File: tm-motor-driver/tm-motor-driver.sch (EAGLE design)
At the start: 17 parts

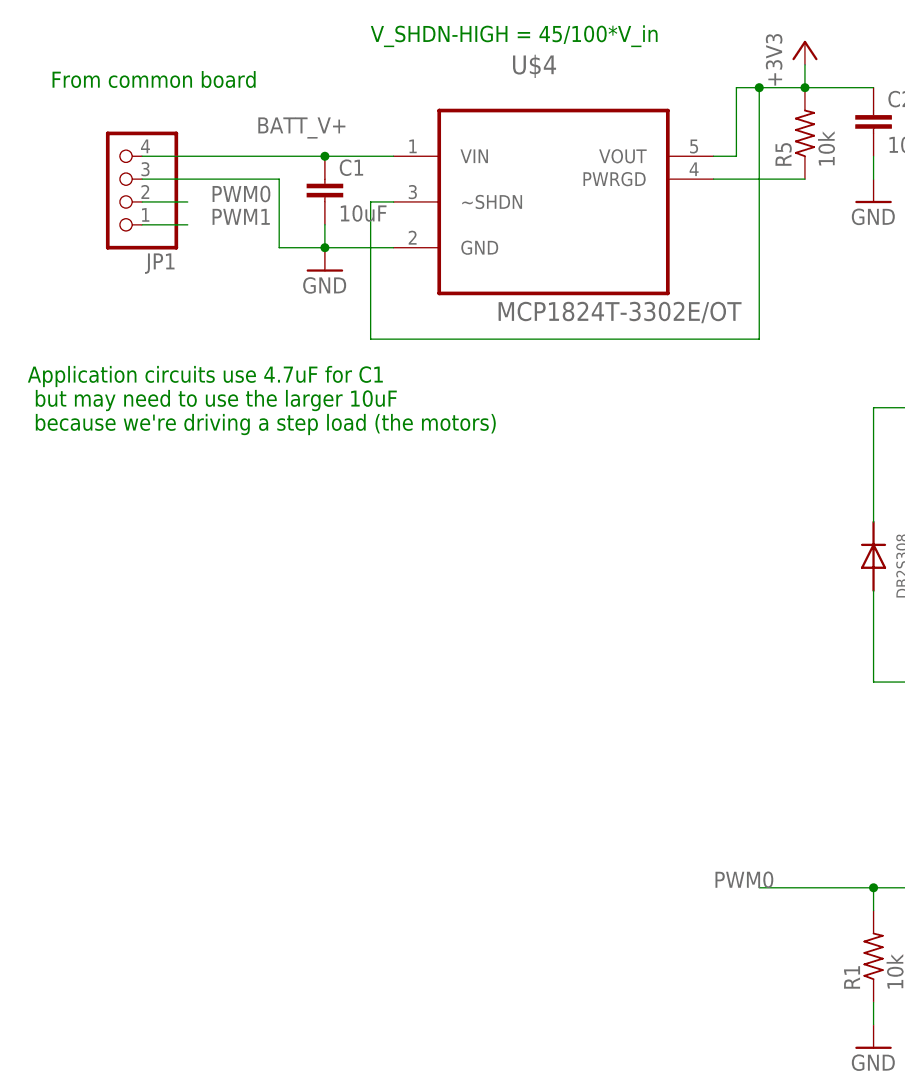
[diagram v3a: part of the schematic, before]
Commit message: Change header to JST
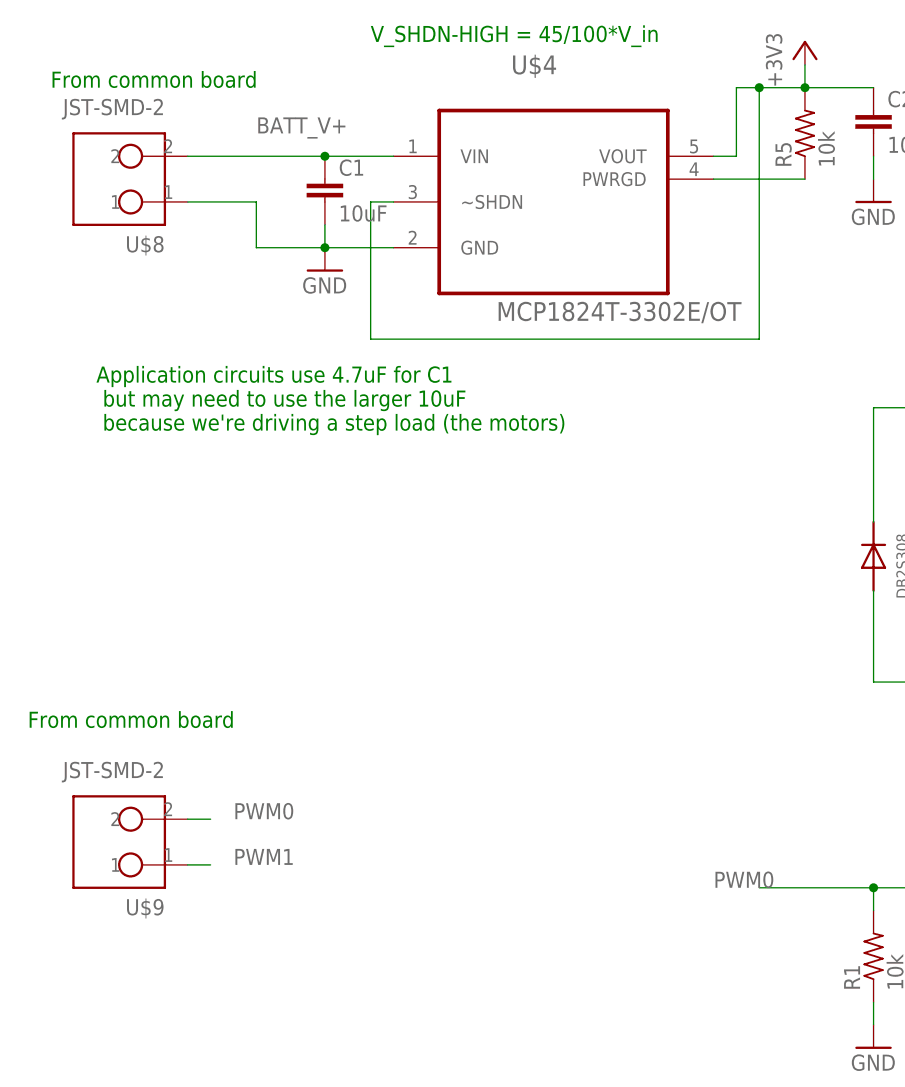
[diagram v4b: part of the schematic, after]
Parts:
- removed JP1: (no value), pinhead:PINHD-1X4
- added U$8, U$9: JST-SMD-2, tactile-music:JST-SMD-2
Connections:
- net BATT_V+: now also U$8.2; no longer JP1.4
- net GND: now also U$8.1; no longer JP1.3
- net PWM0: now also U$9.2; no longer JP1.2
- net PWM1: now also U$9.1; no longer JP1.1
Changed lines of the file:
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@@
 <part name="LED1" library="led" deviceset="LED" device="CHIPLED_0805"/>
 <part name="U$4" library="tactile-music" deviceset="MCP1824T-3302E/OT" device=""/>
-<part name="JP1" library="pinhead" deviceset="PINHD-1X4" device=""/>
 <part name="R2" library="resistor" deviceset="R-US_" device="R0805" value="60"/>
 <part name="GND2" library="supply1" deviceset="GND" device=""/>
@@
 <part name="C2" library="rcl" deviceset="C-EU" device="C0805" value="10uF"/>
 <part name="R5" library="resistor" deviceset="R-US_" device="R0805" value="10k"/>
+<part name="U$8" library="tactile-music" deviceset="JST-SMD-2" device=""/>
+<part name="U$9" library="tactile-music" deviceset="JST-SMD-2" device=""/>
 </parts>
 <sheets>
@@
 <text x="129.54" y="106.68" size="1.778" layer="91">To motor</text>
 <text x="210.82" y="106.68" size="1.778" layer="91">To motor</text>
-<text x="5.08" y="121.92" size="1.778" layer="91">Application circuits use 4.7uF for C1
+<text x="5.08" y="88.9" size="1.778" layer="91">From common board</text>
+<text x="12.7" y="121.92" size="1.778" layer="91">Application circuits use 4.7uF for C1
  but may need to use the larger 10uF
  because we're driving a step load (the motors)</text>
@@
 <instance part="LED1" gate="G$1" x="144.78" y="104.14"/>
 <instance part="U$4" gate="A" x="63.5" y="149.86"/>
-<instance part="JP1" gate="A" x="15.24" y="149.86" rot="R180"/>
 <instance part="R2" gate="G$1" x="144.78" y="114.3" rot="R90"/>
 <instance part="GND2" gate="1" x="99.06" y="53.34"/>
@@
 <instance part="C2" gate="G$1" x="99.06" y="157.48"/>
 <instance part="R5" gate="G$1" x="91.44" y="154.94" rot="R90"/>
+<instance part="U$8" gate="G$1" x="15.24" y="149.86" rot="R180"/>
+<instance part="U$9" gate="G$1" x="15.24" y="76.2" rot="R180"/>
 </instances>
 <busses>
@@
 <net name="BATT_V+" class="0">
 <segment>
-<pinref part="JP1" gate="A" pin="4"/>
 <pinref part="U$4" gate="A" pin="VIN"/>
-<wire x1="17.78" y1="152.4" x2="38.1" y2="152.4" width="0.1524" layer="91"/>
 <label x="30.48" y="154.94" size="1.778" layer="95"/>
 <pinref part="C1" gate="G$1" pin="1"/>
 <wire x1="38.1" y1="152.4" x2="45.72" y2="152.4" width="0.1524" layer="91"/>
+<pinref part="U$8" gate="G$1" pin="2"/>
+<wire x1="38.1" y1="152.4" x2="22.86" y2="152.4" width="0.1524" layer="91"/>
 <junction x="38.1" y="152.4"/>
 </segment>
 </net>
 <net name="PWM0" class="0">
-<segment>
-<pinref part="JP1" gate="A" pin="2"/>
-<wire x1="17.78" y1="147.32" x2="22.86" y2="147.32" width="0.1524" layer="91"/>
-<label x="25.4" y="147.32" size="1.778" layer="95"/>
-</segment>
 <segment>
 <pinref part="U$2" gate="G$1" pin="G"/>
@@
 <label x="81.28" y="71.12" size="1.778" layer="95"/>
 </segment>
+<segment>
+<pinref part="U$9" gate="G$1" pin="2"/>
+<wire x1="22.86" y1="78.74" x2="25.4" y2="78.74" width="0.1524" layer="91"/>
+<label x="27.94" y="78.74" size="1.778" layer="95"/>
+</segment>
 </net>
 <net name="PWM1" class="0">
-<segment>
-<pinref part="JP1" gate="A" pin="1"/>
-<wire x1="17.78" y1="144.78" x2="22.86" y2="144.78" width="0.1524" layer="91"/>
-<label x="25.4" y="144.78" size="1.778" layer="95"/>
-</segment>
 <segment>
 <pinref part="U$6" gate="G$1" pin="G"/>
@@
 <junction x="180.34" y="71.12"/>
 <label x="162.56" y="71.12" size="1.778" layer="95"/>
+</segment>
+<segment>
+<pinref part="U$9" gate="G$1" pin="1"/>
+<wire x1="22.86" y1="73.66" x2="25.4" y2="73.66" width="0.1524" layer="91"/>
+<label x="27.94" y="73.66" size="1.778" layer="95"/>
 </segment>
 </net>
@@
 </segment>
 <segment>
-<pinref part="JP1" gate="A" pin="3"/>
-<wire x1="17.78" y1="149.86" x2="33.02" y2="149.86" width="0.1524" layer="91"/>
-<wire x1="33.02" y1="149.86" x2="33.02" y2="142.24" width="0.1524" layer="91"/>
 <pinref part="U$4" gate="A" pin="GND"/>
-<wire x1="33.02" y1="142.24" x2="38.1" y2="142.24" width="0.1524" layer="91"/>
+<wire x1="30.48" y1="142.24" x2="38.1" y2="142.24" width="0.1524" layer="91"/>
 <pinref part="C1" gate="G$1" pin="2"/>
 <wire x1="38.1" y1="142.24" x2="45.72" y2="142.24" width="0.1524" layer="91"/>
@@
 <junction x="38.1" y="142.24"/>
 <pinref part="GND1" gate="1" pin="GND"/>
+<wire x1="30.48" y1="142.24" x2="30.48" y2="147.32" width="0.1524" layer="91"/>
+<pinref part="U$8" gate="G$1" pin="1"/>
+<wire x1="30.48" y1="147.32" x2="22.86" y2="147.32" width="0.1524" layer="91"/>
 </segment>
 <segment>

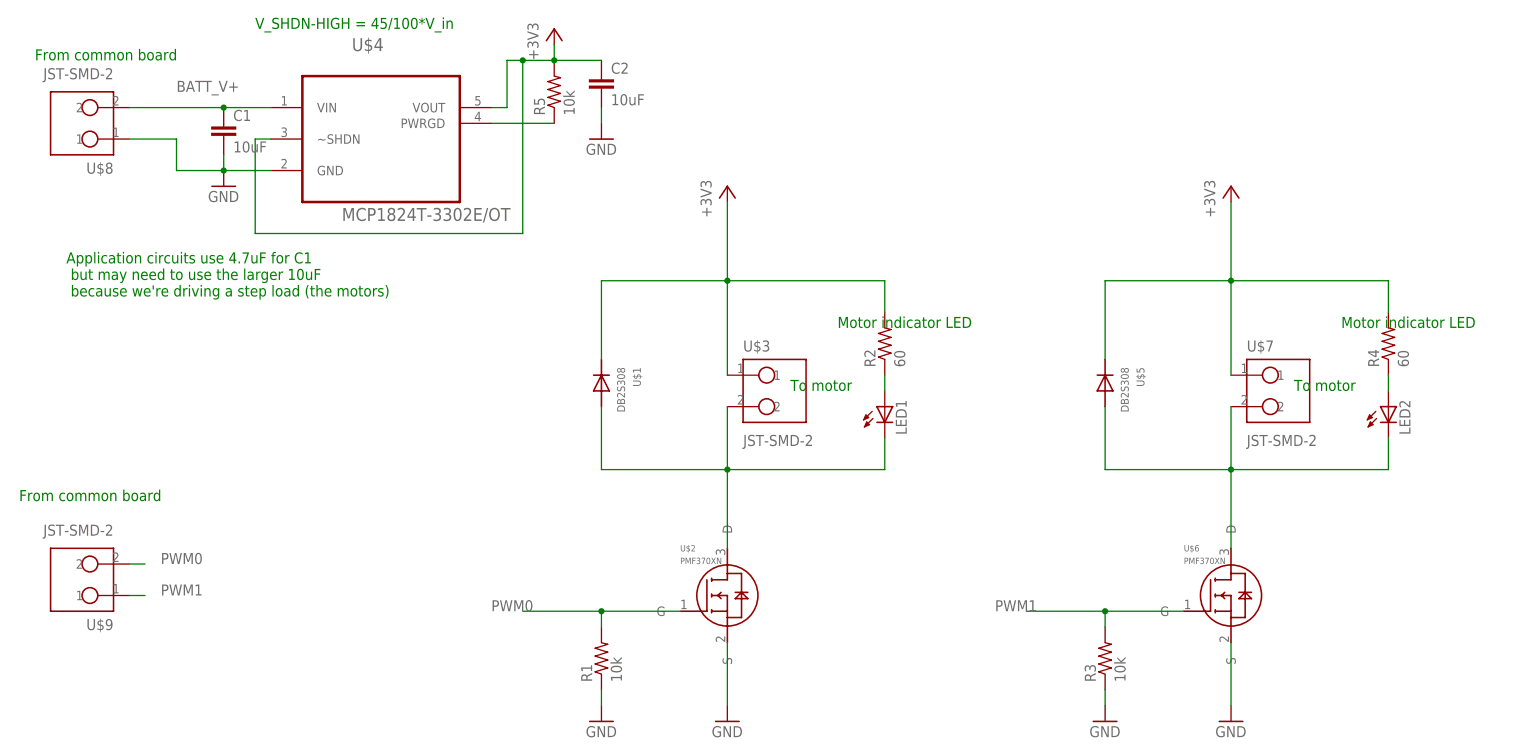
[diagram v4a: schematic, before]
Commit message: Change MOTOR_0 JST connections to make PCB routing easier
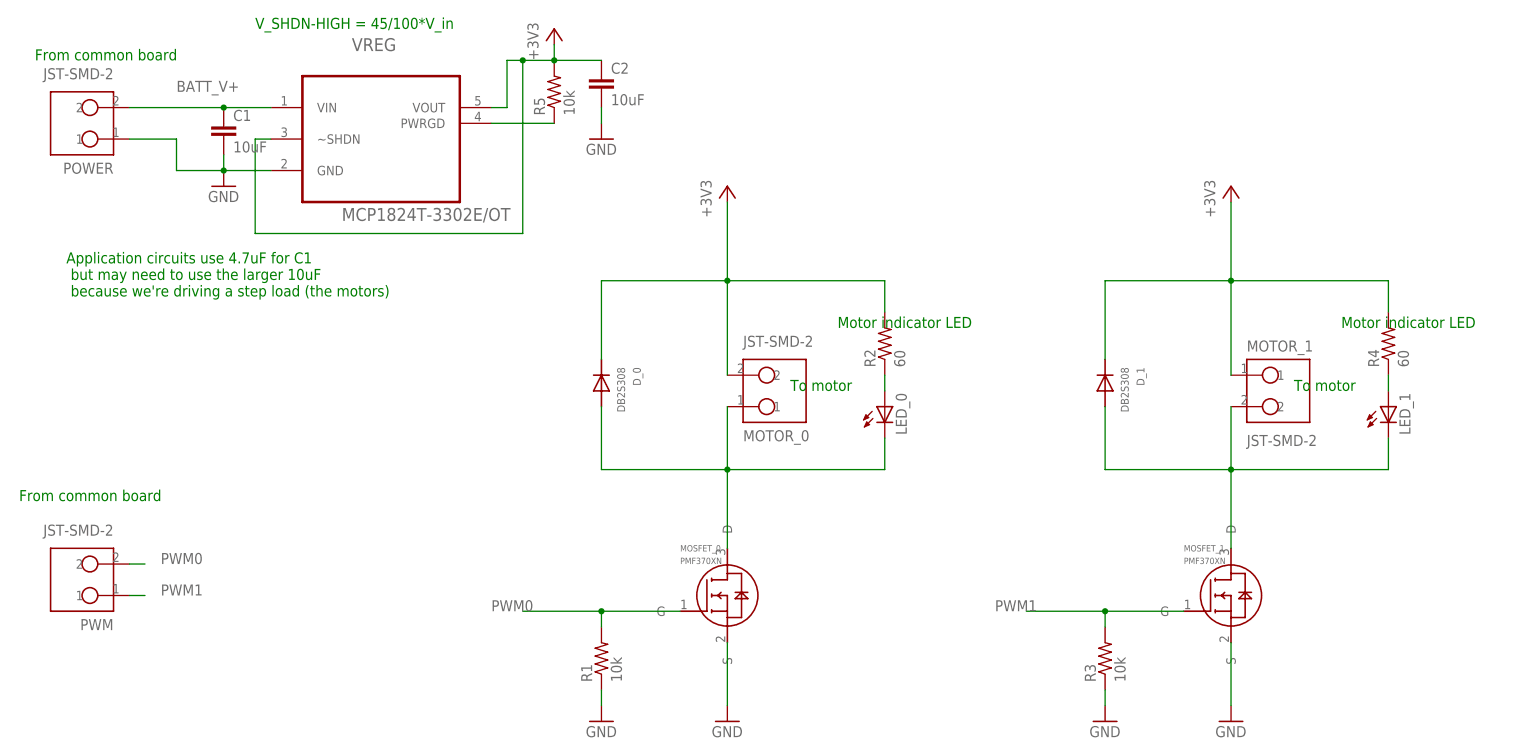
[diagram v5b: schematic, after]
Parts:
- renumbered LED1 to LED_0, LED2 to LED_1, U$1 to D_0, U$2 to MOSFET_0, U$3 to MOTOR_0, U$4 to VREG, U$5 to D_1, U$6 to MOSFET_1, U$7 to MOTOR_1, U$8 to POWER, U$9 to PWM
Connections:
- net +3V3: now also MOTOR_0.2; no longer MOTOR_0.1
- net N$2: now also MOTOR_0.1; no longer MOTOR_0.2

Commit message: Fixed simple schematic errors, and made some PCB fixes / enhancements
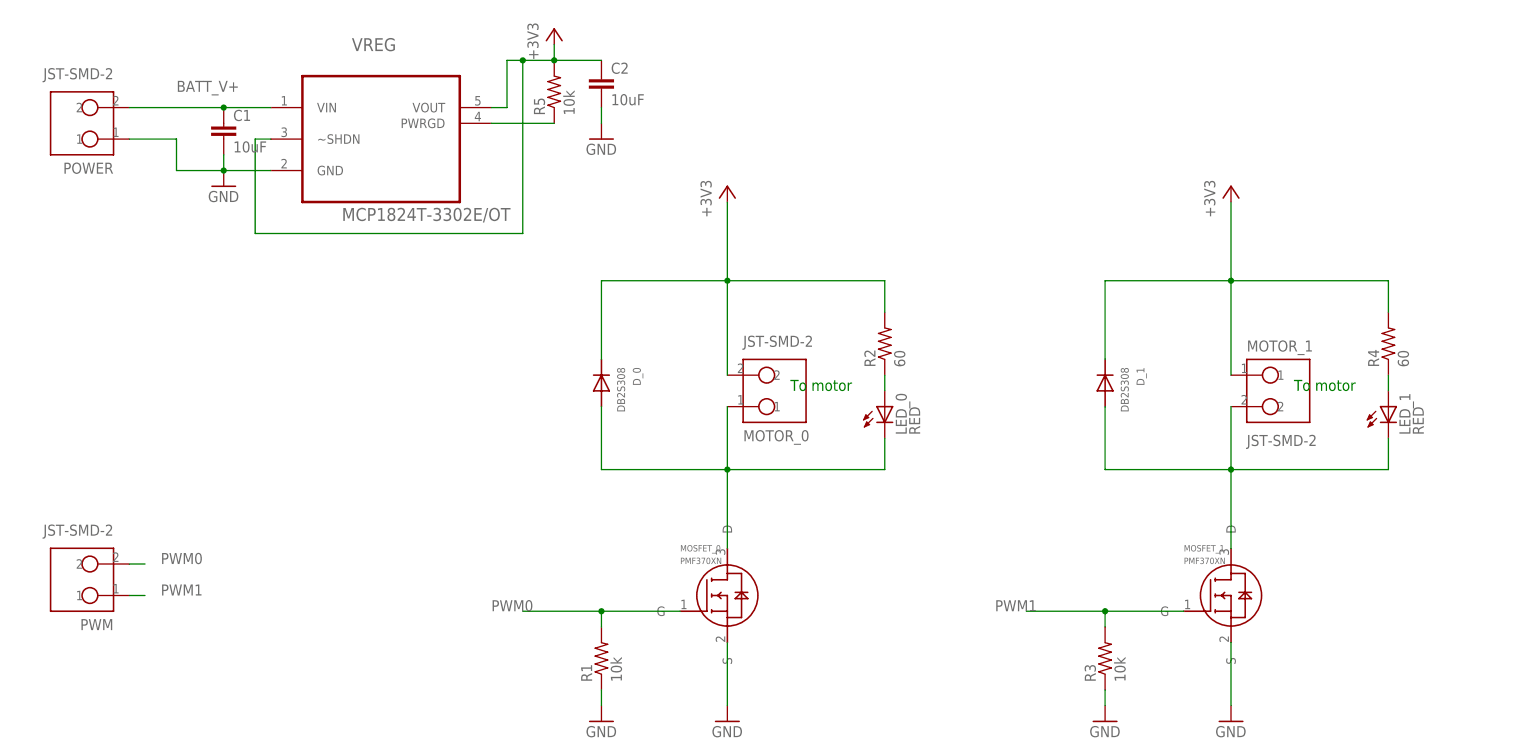
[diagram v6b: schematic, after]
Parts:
- LED_0, LED_1: value (none) -> RED
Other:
- note added: "Diodes are best placed on the motor itself. Attempt that first before soldering diodes on the PCB."
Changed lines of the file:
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@@
 </classes>
 <parts>
-<part name="FRAME1" library="frames" deviceset="DINA4_L" device=""/>
+<part name="FRAME1" library="frames" deviceset="DINA4_L" device="" value="Motor Driver"/>
 <part name="D_0" library="tactile-music" deviceset="DB2S308" device=""/>
 <part name="MOSFET_0" library="tactile-music" deviceset="PMF370XN" device=""/>
 <part name="MOTOR_0" library="tactile-music" deviceset="JST-SMD-2" device=""/>
 <part name="R1" library="resistor" deviceset="R-US_" device="R0805" value="10k"/>
-<part name="LED_0" library="led" deviceset="LED" device="CHIPLED_0805"/>
+<part name="LED_0" library="led" deviceset="LED" device="CHIPLED_0805" value="RED"/>
 <part name="VREG" library="tactile-music" deviceset="MCP1824T-3302E/OT" device=""/>
 <part name="R2" library="resistor" deviceset="R-US_" device="R0805" value="60"/>
@@
 <part name="MOTOR_1" library="tactile-music" deviceset="JST-SMD-2" device=""/>
 <part name="R3" library="resistor" deviceset="R-US_" device="R0805" value="10k"/>
-<part name="LED_1" library="led" deviceset="LED" device="CHIPLED_0805"/>
+<part name="LED_1" library="led" deviceset="LED" device="CHIPLED_0805" value="RED"/>
 <part name="R4" library="resistor" deviceset="R-US_" device="R0805" value="60"/>
 <part name="GND4" library="supply1" deviceset="GND" device=""/>
@@
 <sheet>
 <plain>
-<text x="7.62" y="160.02" size="1.778" layer="91">From common board</text>
-<text x="43.18" y="165.1" size="1.778" layer="91">V_SHDN-HIGH = 45/100*V_in</text>
-<text x="137.16" y="116.84" size="1.778" layer="91">Motor indicator LED</text>
-<text x="218.44" y="116.84" size="1.778" layer="91">Motor indicator LED</text>
+<text x="7.62" y="160.02" size="1.778" layer="98">From common board</text>
+<text x="43.18" y="165.1" size="1.778" layer="98">V_SHDN-HIGH = 45/100*V_in</text>
+<text x="137.16" y="116.84" size="1.778" layer="98">Motor indicator LED</text>
+<text x="218.44" y="116.84" size="1.778" layer="98">Motor indicator LED</text>
 <text x="129.54" y="106.68" size="1.778" layer="91">To motor</text>
 <text x="210.82" y="106.68" size="1.778" layer="91">To motor</text>
-<text x="5.08" y="88.9" size="1.778" layer="91">From common board</text>
-<text x="12.7" y="121.92" size="1.778" layer="91">Application circuits use 4.7uF for C1
+<text x="5.08" y="88.9" size="1.778" layer="98">From common board</text>
+<text x="12.7" y="121.92" size="1.778" layer="98">Application circuits use 4.7uF for C1
  but may need to use the larger 10uF
  because we're driving a step load (the motors)</text>
+<text x="53.34" y="101.6" size="1.778" layer="98">Diodes are best placed
+on the motor itself.
+Attempt that first before
+soldering diodes on the PCB.</text>
+<wire x1="78.74" y1="99.06" x2="78.74" y2="91.44" width="0.1524" layer="98"/>
+<wire x1="78.74" y1="91.44" x2="172.72" y2="91.44" width="0.1524" layer="98"/>
+<wire x1="172.72" y1="91.44" x2="172.72" y2="104.14" width="0.1524" layer="98"/>
+<wire x1="172.72" y1="104.14" x2="177.8" y2="104.14" width="0.1524" layer="98"/>
+<wire x1="177.8" y1="104.14" x2="175.26" y2="106.68" width="0.1524" layer="98"/>
+<wire x1="177.8" y1="104.14" x2="175.26" y2="101.6" width="0.1524" layer="98"/>
+<wire x1="88.9" y1="106.68" x2="93.98" y2="106.68" width="0.1524" layer="98"/>
+<wire x1="91.44" y1="109.22" x2="93.98" y2="106.68" width="0.1524" layer="98"/>
+<wire x1="93.98" y1="106.68" x2="91.44" y2="104.14" width="0.1524" layer="98"/>
 </plain>
 <instances>
